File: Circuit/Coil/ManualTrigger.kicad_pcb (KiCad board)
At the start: 2 copper layers, 3 parts, among them J2 Trigger, SW1 SW_Push

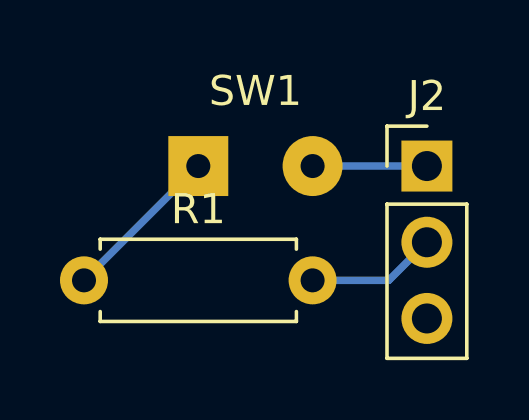
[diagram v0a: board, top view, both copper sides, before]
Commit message: [Circuit] Update circuit files to KiCAD 6's
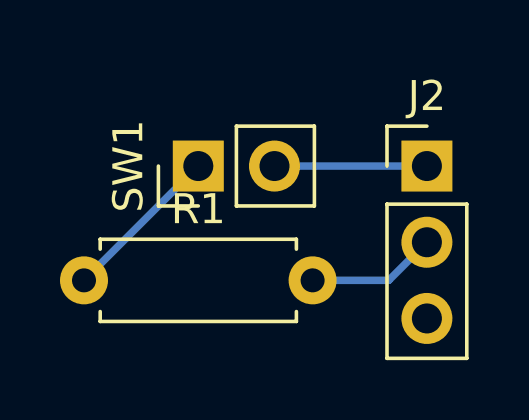
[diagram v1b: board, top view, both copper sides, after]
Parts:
- SW1: footprint Connector_Wire:SolderWirePad_1x02_P3.81mm_Drill0.8mm -> Connector_PinHeader_2.54mm:PinHeader_1x02_P2.54mm_Vertical
- turned SW1 to 90 degrees
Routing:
- net /Trigger+: track 3.81 -> 5.08 mm
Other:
- net class Default removed
